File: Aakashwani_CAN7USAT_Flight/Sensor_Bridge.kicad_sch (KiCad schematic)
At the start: 0 parts

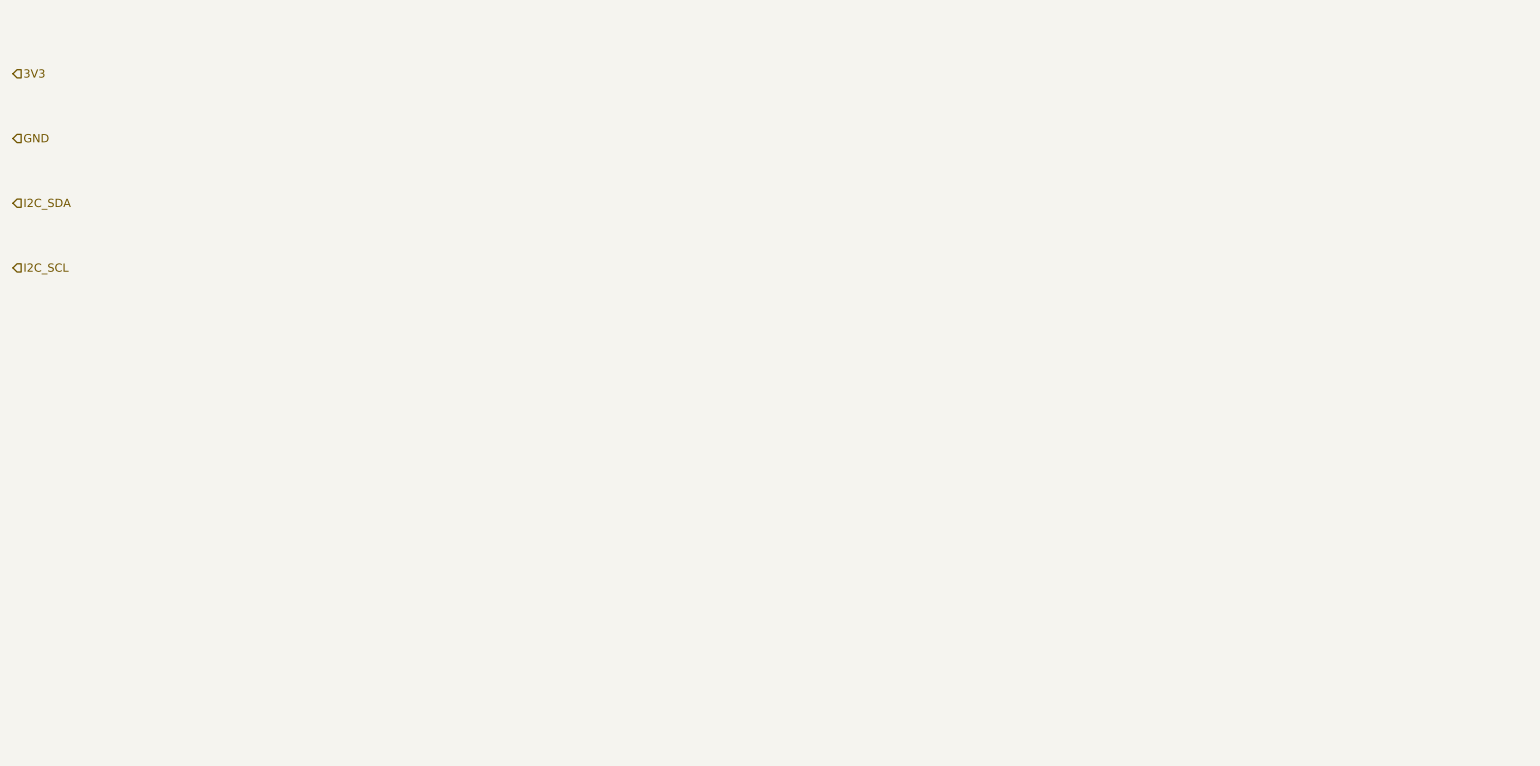
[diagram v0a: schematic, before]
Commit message: feat: Completed Sensor Bridge schematic with I2C bus auto-wiring and IMU failsafes
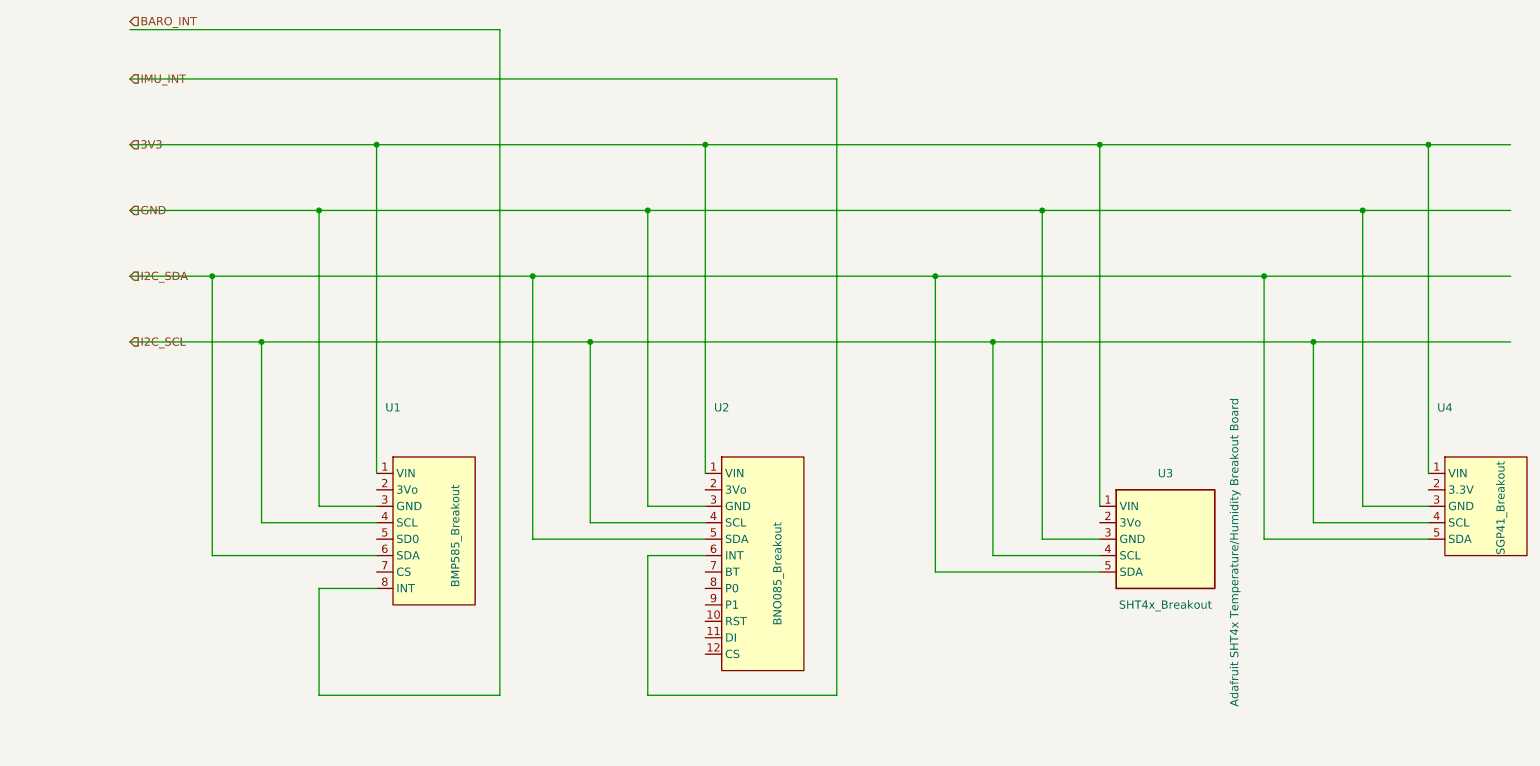
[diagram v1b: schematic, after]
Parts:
- added U1: BMP585_Breakout, Aakashwani_Master:BMP585_Breakout, symbol Aakashwani_Master:BMP585_Breakout
- added U2: BNO085_Breakout, Aakashwani_Master:BNO085_Breakout, symbol Aakashwani_Master:BNO085_Breakout
- added U3: SHT4x_Breakout, CanSat_Library:SHT4x_Breakout, symbol Aakashwani_Master:SHT4x_Breakout
- added U4: SGP41_Breakout, Aakashwani_Master:SGP41_Breakout, symbol Aakashwani_Master:SGP41_Breakout
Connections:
- net 3V3: now also U1.1 (VIN), U2.1 (VIN), U3.1 (VIN), U4.1 (VIN)
- net GND: now also U1.3 (GND), U2.3 (GND), U3.3 (GND), U4.3 (GND)
- net I2C_SCL: now also U1.4 (SCL), U2.4 (SCL), U3.4 (SCL), U4.4 (SCL)
- net I2C_SDA: now also U1.6 (SDA), U2.5 (SDA), U3.5 (SDA), U4.5 (SDA)
- new net IMU_INT: U2.6 (INT)
